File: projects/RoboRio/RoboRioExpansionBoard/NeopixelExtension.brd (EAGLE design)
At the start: 49.2 x 12.7 mm, 5 parts, among them IC2 74HCT125N

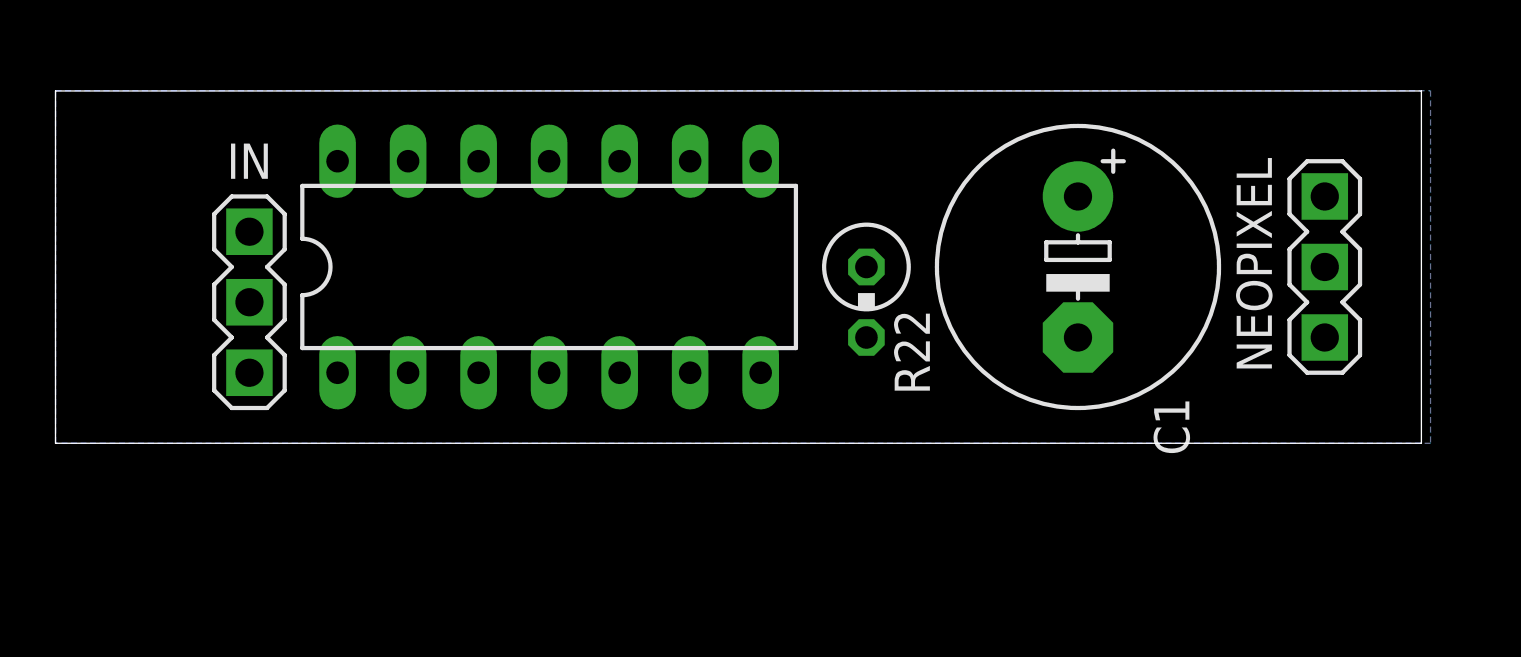
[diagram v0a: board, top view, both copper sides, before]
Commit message: Almost finished neopixel board design
Still has slight issues with the DRC, a couple of traces go to close to
edge of board.
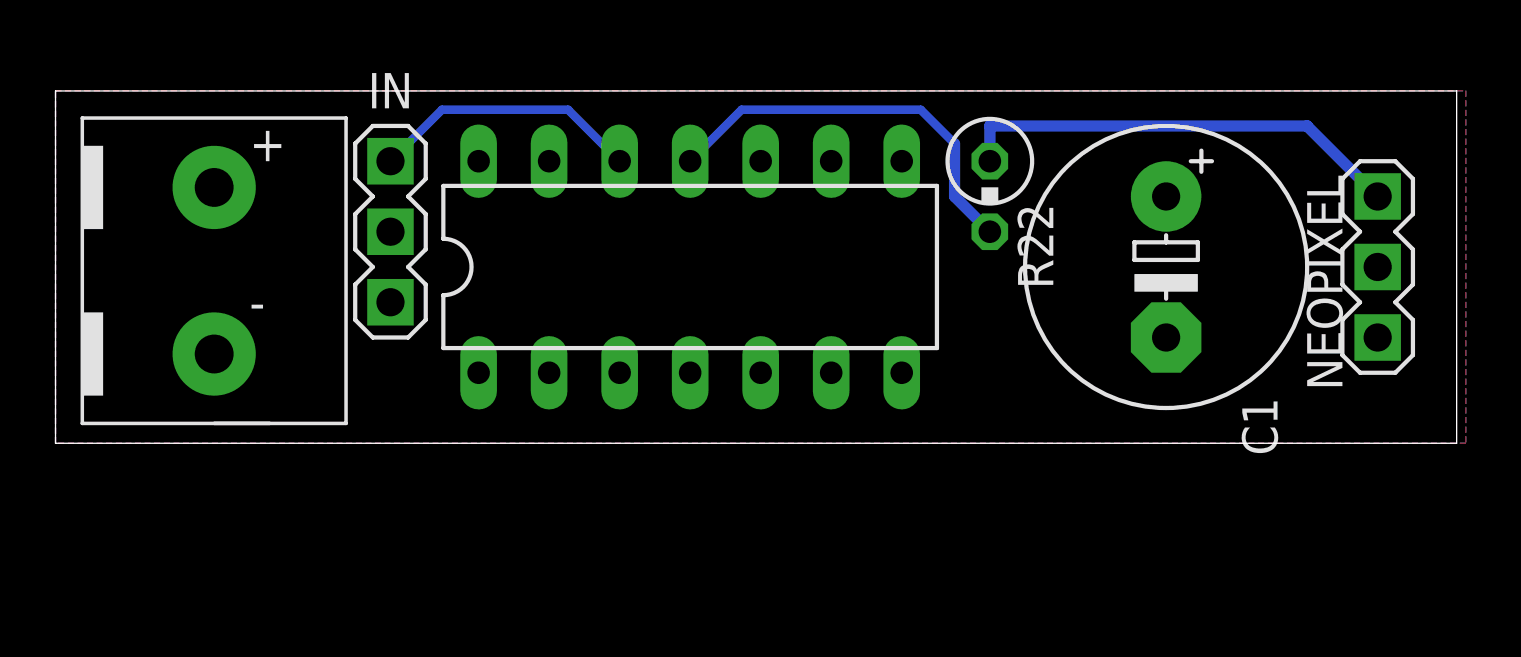
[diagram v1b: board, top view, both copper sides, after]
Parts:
- added U$1: POWER, Molex-39543-0002:POWER
- moved R22 5.85 mm to (33.7, 8.89)
- moved IN 5.68 mm to (12.1, 7.62)
- moved IC2 5.08 mm to (22.9, 6.35)
- moved C1 3.18 mm to (40.0, 6.35)
- moved NEOPIXEL 1.91 mm to (47.6, 6.35)
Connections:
- net GND: now also U$1.GND
- net N$3: now also IC2.12; no longer IC2.2
- net N$4: now also IC2.11; no longer IC2.3
- net VCC: now also U$1.5V
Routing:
- net N$1: track 0.00 -> 16.3 mm
- net N$4: track 0.00 -> 14.5 mm
- net N$3: track 0.00 -> 9.79 mm
- added copper zone on layer 1, net VCC
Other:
- board size 49.2 x 12.7 mm -> 50.5 x 12.7 mm

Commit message: Finished neopixel extension schematic and layout.
Still need to double-check neopixel connector and DRC.
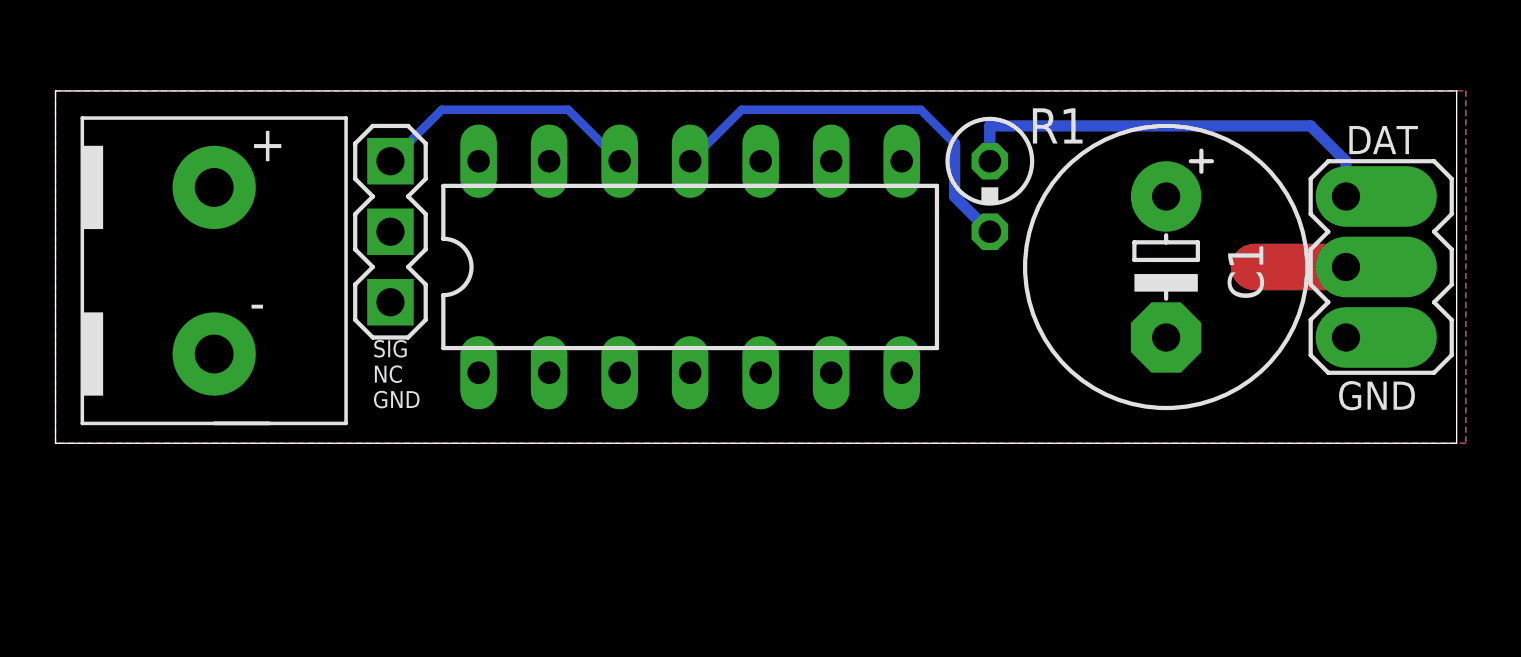
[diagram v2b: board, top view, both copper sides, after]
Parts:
- removed NEOPIXEL: (no value), con-lstb-modified:MA03-1
- added U$2: NEOPIXEL1, NeopixelConnector:NEODIRECTSOLDERORMA03-1
- renumbered R22 to R1
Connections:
- net GND: now also U$2.GND; no longer NEOPIXEL.1
- net N$1: now also U$2.DATA; no longer NEOPIXEL.3
- net VCC: now also U$2.5V; no longer NEOPIXEL.2
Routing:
- net VCC: track 0.00 -> 3.81 mm
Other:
- board text added: "SIG NC GND"
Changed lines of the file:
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@@
 <setting verticaltext="up"/>
 </settings>
-<grid distance="0.05" unitdist="inch" unit="inch" style="lines" multiple="1" display="no" altdistance="0.001" altunitdist="inch" altunit="inch"/>
+<grid distance="0.05" unitdist="inch" unit="inch" style="lines" multiple="1" display="no" altdistance="0.005" altunitdist="inch" altunit="inch"/>
 <layers>
 <layer number="1" name="Top" color="4" fill="1" visible="yes" active="yes"/>
@@
 <layer number="42" name="bRestrict" color="1" fill="10" visible="no" active="yes"/>
 <layer number="43" name="vRestrict" color="2" fill="10" visible="no" active="yes"/>
-<layer number="44" name="Drills" color="7" fill="1" visible="no" active="yes"/>
-<layer number="45" name="Holes" color="7" fill="1" visible="no" active="yes"/>
-<layer number="46" name="Milling" color="3" fill="1" visible="no" active="yes"/>
-<layer number="47" name="Measures" color="7" fill="1" visible="no" active="yes"/>
-<layer number="48" name="Document" color="7" fill="1" visible="no" active="yes"/>
-<layer number="49" name="Reference" color="7" fill="1" visible="no" active="yes"/>
+<layer number="44" name="Drills" color="7" fill="1" visible="yes" active="yes"/>
+<layer number="45" name="Holes" color="7" fill="1" visible="yes" active="yes"/>
+<layer number="46" name="Milling" color="3" fill="1" visible="yes" active="yes"/>
+<layer number="47" name="Measures" color="7" fill="1" visible="yes" active="yes"/>
+<layer number="48" name="Document" color="7" fill="1" visible="yes" active="yes"/>
+<layer number="49" name="Reference" color="7" fill="1" visible="yes" active="yes"/>
 <layer number="50" name="dxf" color="7" fill="1" visible="no" active="no"/>
-<layer number="51" name="tDocu" color="7" fill="1" visible="no" active="yes"/>
-<layer number="52" name="bDocu" color="7" fill="1" visible="no" active="yes"/>
+<layer number="51" name="tDocu" color="7" fill="1" visible="yes" active="yes"/>
+<layer number="52" name="bDocu" color="7" fill="1" visible="yes" active="yes"/>
 <layer number="53" name="tGND_GNDA" color="7" fill="9" visible="no" active="no"/>
 <layer number="54" name="bGND_GNDA" color="1" fill="9" visible="no" active="no"/>
@@
 <layer number="99" name="SpiceOrder" color="5" fill="1" visible="no" active="no"/>
 <layer number="100" name="Muster" color="7" fill="1" visible="no" active="no"/>
-<layer number="101" name="Patch_Top" color="12" fill="4" visible="no" active="yes"/>
-<layer number="102" name="Vscore" color="7" fill="1" visible="no" active="yes"/>
-<layer number="103" name="fp3" color="7" fill="1" visible="no" active="yes"/>
-<layer number="104" name="Name" color="7" fill="1" visible="no" active="yes"/>
+<layer number="101" name="Patch_Top" color="12" fill="4" visible="yes" active="yes"/>
+<layer number="102" name="Vscore" color="7" fill="1" visible="yes" active="yes"/>
+<layer number="103" name="fp3" color="7" fill="1" visible="yes" active="yes"/>
+<layer number="104" name="Name" color="7" fill="1" visible="yes" active="yes"/>
 <layer number="105" name="Beschreib" color="9" fill="1" visible="no" active="yes"/>
 <layer number="106" name="BGA-Top" color="4" fill="1" visible="no" active="yes"/>
@@
 <wire x1="50.47" y1="12.69" x2="0" y2="12.69" width="0" layer="20"/>
 <wire x1="0" y1="12.69" x2="0" y2="0" width="0" layer="20"/>
+<text x="11.43" y="1.27" size="0.6096" layer="25">SIG
+NC
+GND</text>
 </plain>
 <attributes>
@@
 <attribute name="VALUE" x="16.129" y="5.715" size="1.27" layer="27" ratio="10"/>
 </element>
-<element name="NEOPIXEL" library="con-lstb-modified" package="MA03-1" value="" x="47.625" y="6.35" smashed="yes" rot="R90">
-<attribute name="OC_NEWARK" value="unknown" x="47.625" y="6.35" size="1.778" layer="27" rot="R90" display="off"/>
-<attribute name="MPN" value="" x="47.625" y="6.35" size="1.778" layer="27" rot="R90" display="off"/>
-<attribute name="MF" value="" x="47.625" y="6.35" size="1.778" layer="27" rot="R90" display="off"/>
-<attribute name="OC_FARNELL" value="unknown" x="47.625" y="6.35" size="1.778" layer="27" rot="R90" display="off"/>
-<attribute name="NAME" x="45.72" y="1.905" size="1.27" layer="25" ratio="10" rot="R90" align="center-left"/>
+<element name="R1" library="resistor" package="0309V" value="470" x="33.655" y="8.89" smashed="yes" rot="R270">
+<attribute name="NAME" x="35.052" y="10.795" size="1.27" layer="25" ratio="10"/>
+<attribute name="VALUE" x="32.004" y="5.2832" size="1.27" layer="27" ratio="10"/>
 </element>
-<element name="R22" library="resistor" package="0309V" value="470" x="33.655" y="8.89" rot="R270"/>
 <element name="IN" library="con-lstb-modified" package="MA03-1" value="" x="12.065" y="7.62" smashed="yes" rot="R90">
 <attribute name="OC_NEWARK" value="unknown" x="12.065" y="7.62" size="1.778" layer="27" rot="R90" display="off"/>
@@
 <attribute name="MF" value="" x="12.065" y="7.62" size="1.778" layer="27" rot="R90" display="off"/>
 <attribute name="OC_FARNELL" value="unknown" x="12.065" y="7.62" size="1.778" layer="27" rot="R90" display="off"/>
-<attribute name="NAME" x="12.065" y="12.7" size="1.27" layer="25" ratio="10" align="center"/>
 </element>
-<element name="C1" library="adafruit" package="E5-10,5" value="1000uf" x="40.005" y="6.35" rot="R270"/>
+<element name="C1" library="adafruit" package="E5-10,5" value="1000uf" x="40.005" y="6.35" smashed="yes" rot="R270">
+<attribute name="NAME" x="42.2402" y="7.239" size="1.27" layer="25" ratio="10" rot="R270"/>
+<attribute name="VALUE" x="36.7792" y="9.4742" size="1.27" layer="27" ratio="10" rot="R270"/>
+</element>
 <element name="U$1" library="Molex-39543-0002" package="POWER" value="POWER" x="5.715" y="5.715"/>
+<element name="U$2" library="NeopixelConnector" package="NEODIRECTSOLDERORMA03-1" value="NEOPIXEL1" x="46.482" y="6.35" smashed="yes" rot="R270"/>
 </elements>
 <signals>
 <signal name="N$1">
-<contactref element="NEOPIXEL" pad="3"/>
-<contactref element="R22" pad="1"/>
+<contactref element="R1" pad="1"/>
 <wire x1="33.655" y1="10.16" x2="33.655" y2="11.43" width="0.4064" layer="16"/>
-<wire x1="33.655" y1="11.43" x2="45.085" y2="11.43" width="0.4064" layer="16"/>
-<wire x1="45.085" y1="11.43" x2="47.625" y2="8.89" width="0.4064" layer="16"/>
+<wire x1="33.655" y1="11.43" x2="45.212" y2="11.43" width="0.4064" layer="16"/>
+<contactref element="U$2" pad="DATA"/>
+<wire x1="45.212" y1="11.43" x2="46.482" y2="10.16" width="0.4064" layer="16"/>
+<wire x1="46.482" y1="10.16" x2="46.482" y2="8.89" width="0.4064" layer="16"/>
 </signal>
 <signal name="GND">
@@
 <contactref element="IC2" pad="13"/>
 <contactref element="IC2" pad="7"/>
-<contactref element="NEOPIXEL" pad="1"/>
 <contactref element="IC2" pad="4"/>
 <contactref element="IC2" pad="10"/>
 <contactref element="IC2" pad="1"/>
 <contactref element="C1" pad="-"/>
-<polygon width="0.4064" layer="16" isolate="0.254">
+<polygon width="0.4064" layer="16">
 <vertex x="50.8" y="12.7"/>
 <vertex x="50.8" y="0"/>
@@
 </polygon>
 <contactref element="U$1" pad="GND"/>
+<contactref element="U$2" pad="GND"/>
 </signal>
 <signal name="N$3">
@@
 <signal name="N$4">
 <contactref element="IC2" pad="11"/>
-<contactref element="R22" pad="2"/>
+<contactref element="R1" pad="2"/>
 <wire x1="22.86" y1="10.16" x2="24.7142" y2="12.0142" width="0.3048" layer="16"/>
 <wire x1="24.7142" y1="12.0142" x2="31.1658" y2="12.0142" width="0.3048" layer="16"/>
@@
 <signal name="VCC">
 <contactref element="IC2" pad="14"/>
-<contactref element="NEOPIXEL" pad="2"/>
 <contactref element="C1" pad="+"/>
 <contactref element="U$1" pad="5V"/>
@@
 <vertex x="0" y="0"/>
 </polygon>
+<contactref element="U$2" pad="5V"/>
+<wire x1="46.99" y1="6.35" x2="43.18" y2="6.35" width="1.6764" layer="1"/>
 </signal>
 </signals>
 </board>
 </drawing>
+<compatibility>
+<note version="6.3" minversion="6.2.2" severity="warning">
+Since Version 6.2.2 text objects can contain more than one line,
+which will not be processed correctly with this version.
+</note>
+</compatibility>
 </eagle>

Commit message: Updated neopixel connector
to use AND gate for level shifter
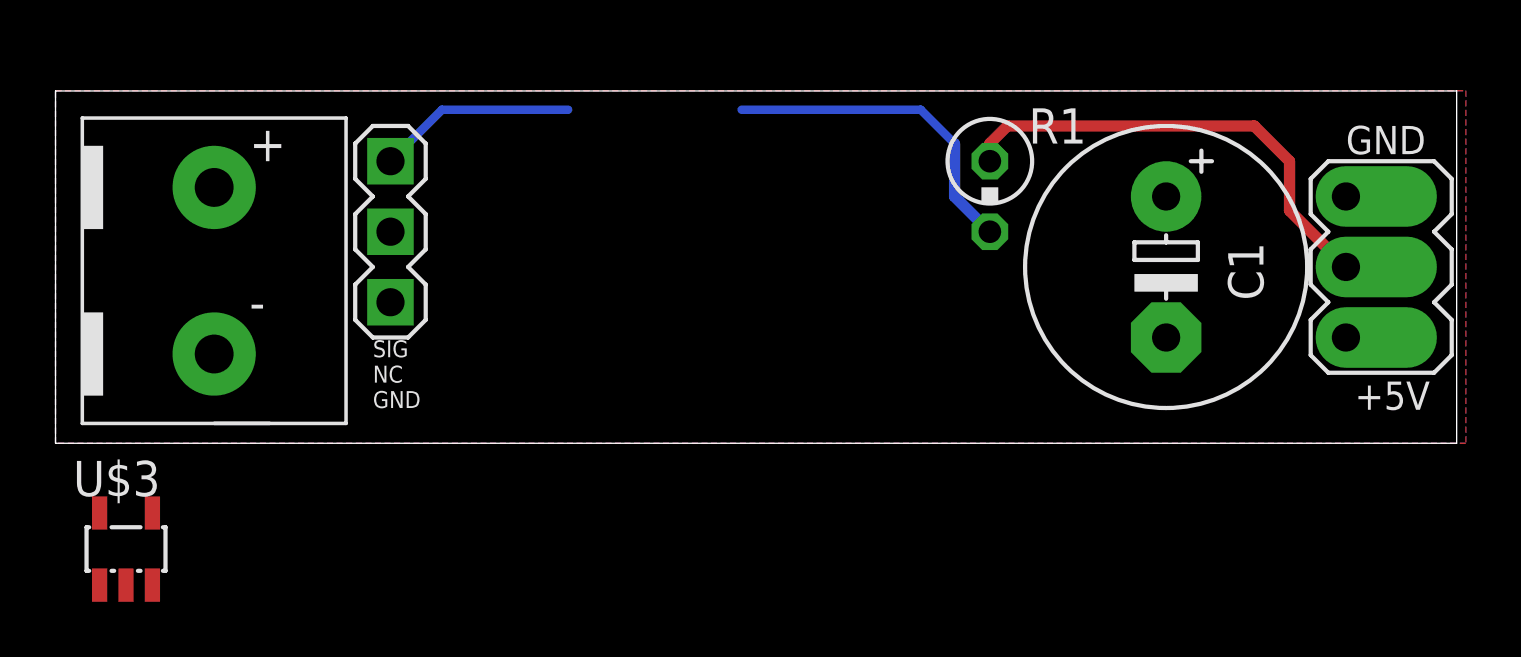
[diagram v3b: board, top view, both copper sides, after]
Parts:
- removed IC2: 74HCT125N, 74xx-eu:DIL14
- added U$3: 74AHCT1G08, SOT25:SOT25
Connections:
- net GND: now also U$3.3; no longer IC2.1, IC2.10, IC2.13, IC2.4, IC2.7
- net N$3: no longer IC2.12
- net N$4: now also U$3.4; no longer IC2.11
- net VCC: now also U$3.2, U$3.5; no longer IC2.14
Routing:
- net VCC: track 3.81 -> 0.00 mm
- net N$4: track 14.5 -> 11.9 mm
- net N$3: track 9.79 -> 7.17 mm
- net N$1: track 15.9 -> 16.9 mm
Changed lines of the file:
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@@
 </autorouter>
 <elements>
-<element name="IC2" library="74xx-eu" package="DIL14" value="74HCT125N" x="22.86" y="6.35" smashed="yes">
-<attribute name="VALUE" x="16.129" y="5.715" size="1.27" layer="27" ratio="10"/>
-</element>
 <element name="R1" library="resistor" package="0309V" value="470" x="33.655" y="8.89" smashed="yes" rot="R270">
 <attribute name="NAME" x="35.052" y="10.795" size="1.27" layer="25" ratio="10"/>
@@
 <element name="U$1" library="Molex-39543-0002" package="POWER" value="POWER" x="5.715" y="5.715"/>
 <element name="U$2" library="NeopixelConnector" package="NEODIRECTSOLDERORMA03-1" value="NEOPIXEL1" x="46.482" y="6.35" smashed="yes" rot="R270"/>
+<element name="U$3" library="SOT25" package="SOT25" value="74AHCT1G08" x="2.54" y="-3.81"/>
 </elements>
 <signals>
 <signal name="N$1">
 <contactref element="R1" pad="1"/>
-<wire x1="33.655" y1="10.16" x2="33.655" y2="11.43" width="0.4064" layer="16"/>
-<wire x1="33.655" y1="11.43" x2="45.212" y2="11.43" width="0.4064" layer="16"/>
 <contactref element="U$2" pad="DATA"/>
-<wire x1="45.212" y1="11.43" x2="46.482" y2="10.16" width="0.4064" layer="16"/>
-<wire x1="46.482" y1="10.16" x2="46.482" y2="8.89" width="0.4064" layer="16"/>
+<wire x1="33.655" y1="10.16" x2="33.655" y2="10.795" width="0.4064" layer="1"/>
+<wire x1="33.655" y1="10.795" x2="34.29" y2="11.43" width="0.4064" layer="1"/>
+<wire x1="34.29" y1="11.43" x2="43.18" y2="11.43" width="0.4064" layer="1"/>
+<wire x1="43.18" y1="11.43" x2="44.45" y2="10.16" width="0.4064" layer="1"/>
+<wire x1="44.45" y1="10.16" x2="44.45" y2="8.382" width="0.4064" layer="1"/>
+<wire x1="44.45" y1="8.382" x2="46.482" y2="6.35" width="0.4064" layer="1"/>
 </signal>
 <signal name="GND">
 <contactref element="IN" pad="1"/>
-<contactref element="IC2" pad="13"/>
-<contactref element="IC2" pad="7"/>
-<contactref element="IC2" pad="4"/>
-<contactref element="IC2" pad="10"/>
-<contactref element="IC2" pad="1"/>
 <contactref element="C1" pad="-"/>
 <polygon width="0.4064" layer="16">
@@
 <contactref element="U$1" pad="GND"/>
 <contactref element="U$2" pad="GND"/>
+<contactref element="U$3" pad="3"/>
+<wire x1="40.005" y1="3.81" x2="46.482" y2="8.89" width="0" layer="19" extent="1-1"/>
+<wire x1="12.065" y1="5.08" x2="40.005" y2="3.81" width="0" layer="19" extent="1-1"/>
+<wire x1="5.715" y1="3.215" x2="12.065" y2="5.08" width="0" layer="19" extent="1-1"/>
+<wire x1="3.49" y1="-5.11" x2="5.715" y2="3.215" width="0" layer="19" extent="1-1"/>
 </signal>
 <signal name="N$3">
-<contactref element="IC2" pad="12"/>
 <contactref element="IN" pad="3"/>
 <wire x1="12.065" y1="10.16" x2="13.9192" y2="12.0142" width="0.3048" layer="16"/>
 <wire x1="13.9192" y1="12.0142" x2="18.4658" y2="12.0142" width="0.3048" layer="16"/>
-<wire x1="18.4658" y1="12.0142" x2="20.32" y2="10.16" width="0.3048" layer="16"/>
 </signal>
 <signal name="N$4">
-<contactref element="IC2" pad="11"/>
 <contactref element="R1" pad="2"/>
-<wire x1="22.86" y1="10.16" x2="24.7142" y2="12.0142" width="0.3048" layer="16"/>
 <wire x1="24.7142" y1="12.0142" x2="31.1658" y2="12.0142" width="0.3048" layer="16"/>
 <wire x1="31.1658" y1="12.0142" x2="32.385" y2="10.795" width="0.3048" layer="16"/>
 <wire x1="32.385" y1="10.795" x2="32.385" y2="8.89" width="0.4064" layer="16"/>
 <wire x1="32.385" y1="8.89" x2="33.655" y2="7.62" width="0.4064" layer="16"/>
+<contactref element="U$3" pad="4"/>
+<wire x1="3.49" y1="-2.51" x2="24.7142" y2="12.0142" width="0" layer="19" extent="1-16"/>
 </signal>
 <signal name="VCC">
-<contactref element="IC2" pad="14"/>
 <contactref element="C1" pad="+"/>
 <contactref element="U$1" pad="5V"/>
@@
 </polygon>
 <contactref element="U$2" pad="5V"/>
-<wire x1="46.99" y1="6.35" x2="43.18" y2="6.35" width="1.6764" layer="1"/>
+<contactref element="U$3" pad="5"/>
+<contactref element="U$3" pad="2"/>
+<wire x1="40.005" y1="8.89" x2="46.482" y2="3.81" width="0" layer="19" extent="1-1"/>
+<wire x1="5.715" y1="9.215" x2="40.005" y2="8.89" width="0" layer="19" extent="1-1"/>
+<wire x1="1.59" y1="-2.51" x2="5.715" y2="9.215" width="0" layer="19" extent="1-1"/>
+<wire x1="2.54" y1="-5.11" x2="1.59" y2="-2.51" width="0" layer="19" extent="1-1"/>
 </signal>
 </signals>
